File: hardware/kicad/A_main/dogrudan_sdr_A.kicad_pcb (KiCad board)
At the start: 6 copper layers, 235 x 225 mm, 264 parts, among them J1 XT60, J10 JTAG 2x3, J20 SMA A1, J21 SMA B1, J22 SMA A2, J23 SMA B2, J30 SMA TX1, J31 SMA TX2, J32 SMA TX3, J33 SMA TX4, J40 HR911130A, J41 HR911130A, J60 GPS modul, J61 SMA 10MHz ref, J62 DAC modul, J63 C kartina, J64 UART 3.3V, J65 C kartina #2, J66 D kartina, Q1 DMP3098L, SW1 PROG, T1 ADT1-1WT+, T10 ADT1-1WT+, T11 ADT1-1WT+, T12 ADT1-1WT+, T13 ADT1-1WT+, T2 ADT1-1WT+, T3 ADT1-1WT+, T4 ADT1-1WT+, U1 TPS62130, U10 LFE5U-25F-7BG256I, U11 W25Q128JVSIQ, U15 ADCLK846BCPZ, U16 SN65LVDS2DBVR, U17 SN65LVDS2DBVR, U2 TPS62130, U20 AD9251BCPZ-80, U21 AD9251BCPZ-80, U3 TPS7A2033, U30 AD9767ASTZ, U31 AD9767ASTZ, U4 ADP150, U40 RTL8211FI-CG, U41 RTL8211FI-CG, U5 ADP150, U50 W9825G6KH-6I, U6 ADP150, U62 TLV3501AIDBVR, U7 ADP150, U8 ADP150, U9 ADP150, Y10 ABLNO-V-80.000MHZ, Y610 25MHz, Y626 25MHz

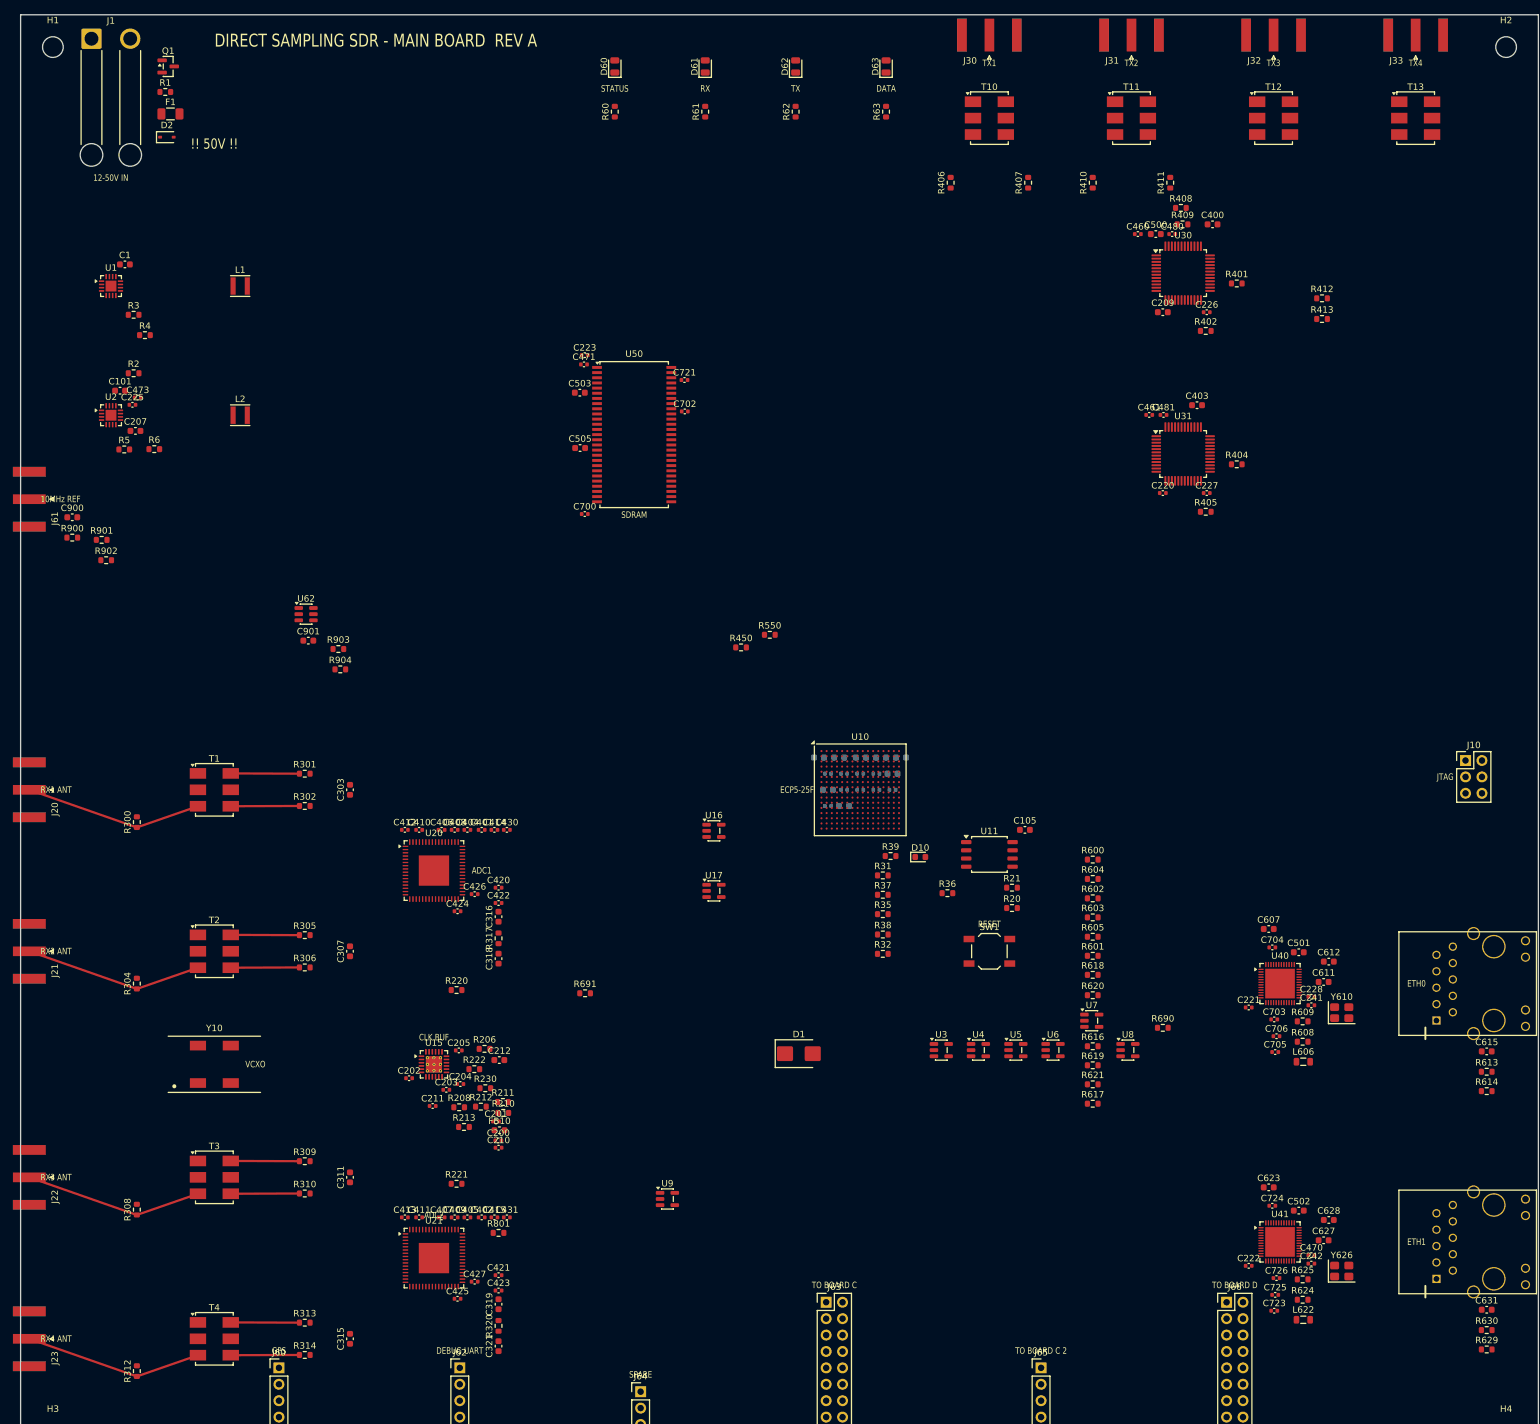
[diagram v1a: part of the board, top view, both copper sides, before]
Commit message: Connect the pads that had no net
A symbol pin number must agree with the footprint pad number. If the
numbers do not agree, the net goes nowhere. The netlist removes it
and gives no message. ERC examines the schematic and sees a wire. DRC
does not count an unconnected pad as a violation. All three boards
showed zero ERC violations while 31 pads had no net.

Two of these faults stopped a board.

The footprint of the Ethernet PHY was for a different part. The
project used QFN-48 6x6 mm with 0.4 mm pitch. The RTL8211F(I)-CG is
WQFN-40-EP 5x5 mm. You cannot solder the part to that pad pattern.

The 25 MHz crystal had a 2-pin symbol on a 4-pad footprint. On a 3225
crystal the terminals are the diagonal pads 1 and 3. Pads 2 and 4 are
the metal can. XO went to pad 2. There was no crystal between XI and
XO, and thus neither PHY could make a clock.

The paddle of the AD9251 was pin 0 in the symbol and pad 65 in the
footprint. The paddle of the PE4312 was Pad against pad 21. The gas
discharge tubes had one electrode unconnected, because
Device:GDT_2Pin uses pins 1 and 3 but the varistor footprint uses
pads 1 and 2. A local footprint with pads 1 and 3 corrects this.

ped_denetim.py finds these faults on the board. yap.sh runs it before
the DSN export. The chain stops if a pad has no net.

The DSN export also changed. It declared In1 and In4 as power layers
but did not export the copper on them. The router thus believed that
the two ground planes were empty. It routed the 289 pins of GND as
traces on the signal layers. The planes now go out as conduction
areas.
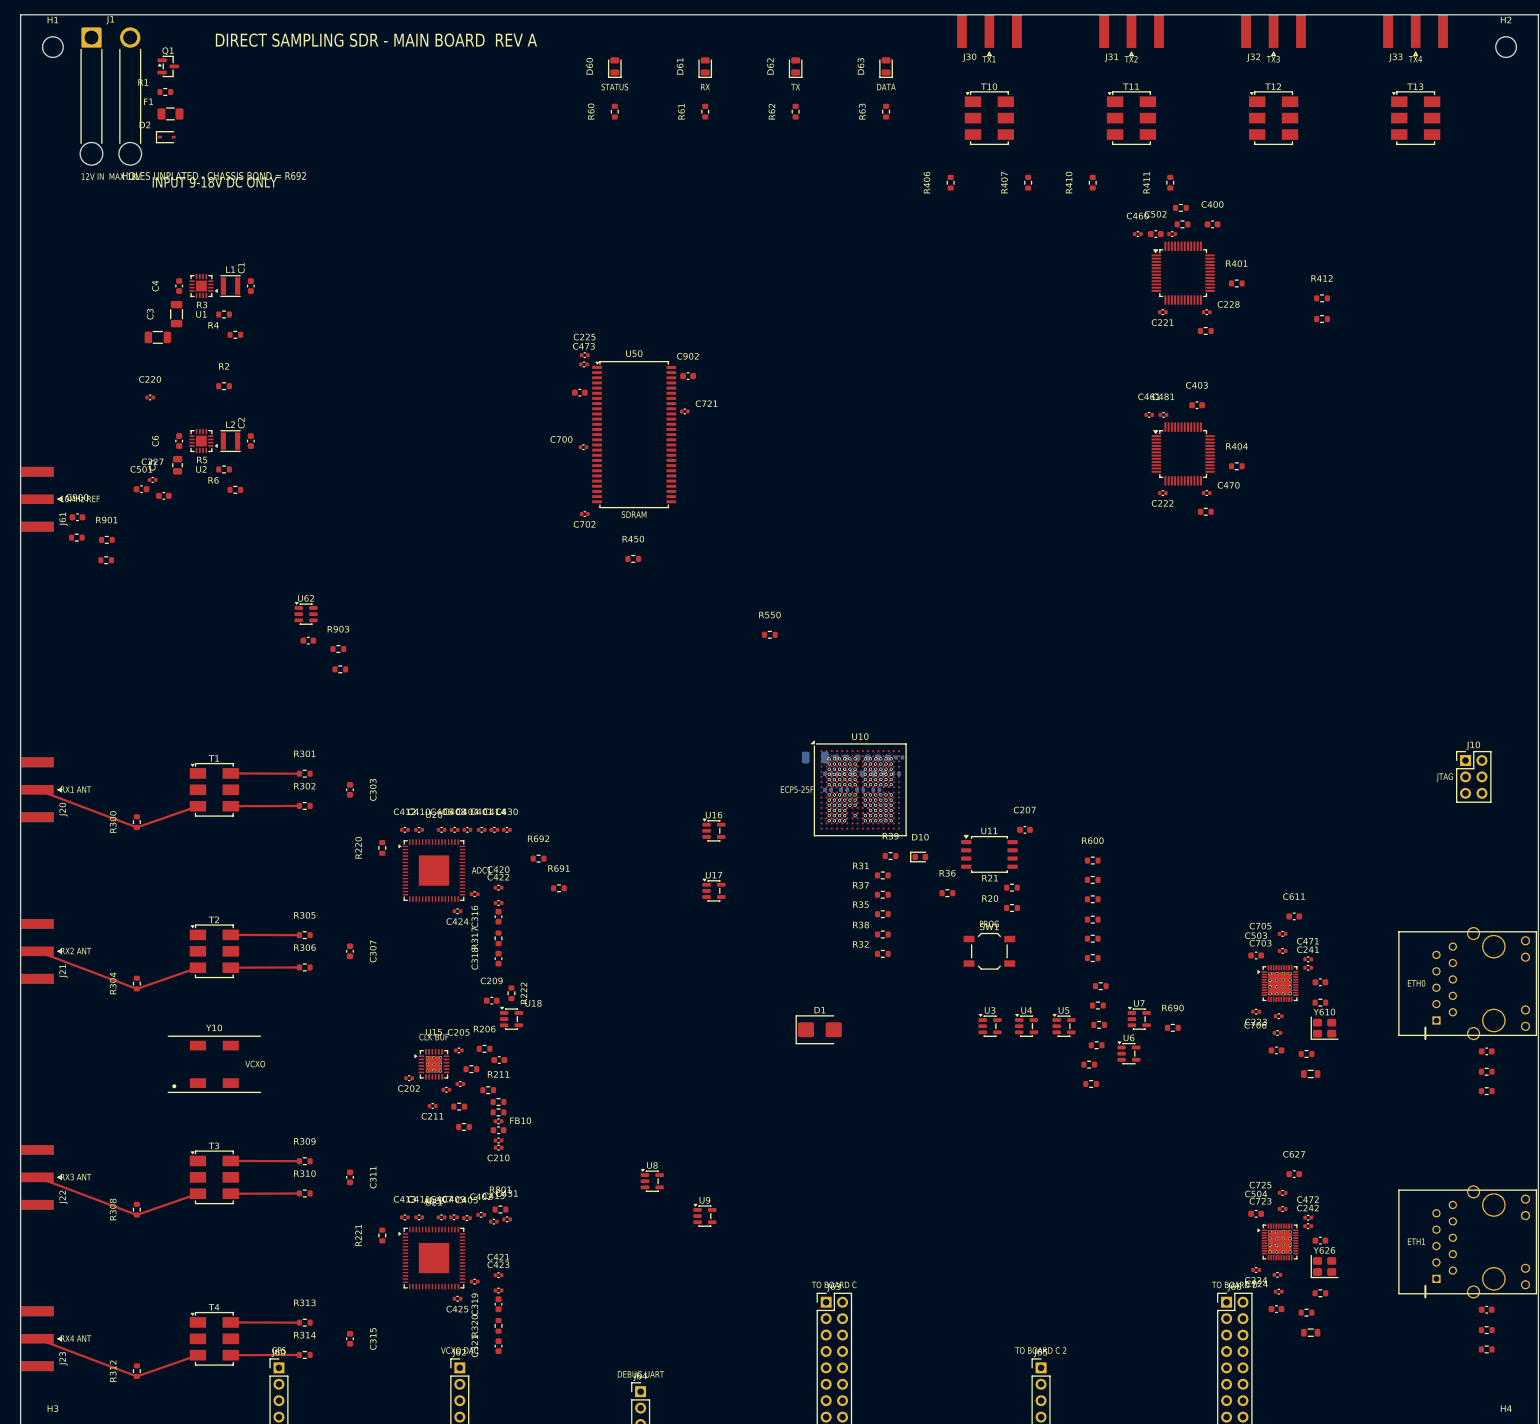
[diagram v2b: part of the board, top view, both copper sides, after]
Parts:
- added C3: 10uF, C_1206_3216Metric, F.Cu at (24.1, 46.4)
- added C4: 100nF, C_0603_1608Metric, F.Cu at (24.6, 42.0)
- added C5: 10uF, C_0805_2012Metric, F.Cu at (24.3, 69.8)
- added C6: 100nF, C_0603_1608Metric, F.Cu at (24.6, 66.0)
- added R692: 0R, R_0603_1608Metric, F.Cu at (80.2, 130.7)
- added U18: SN65LVDS2DBVR, SOT-23-5, F.Cu at (76.0, 155.5)
- C100: footprint C_0603_1608Metric -> C_1206_3216Metric
- C104: footprint C_0603_1608Metric -> C_1206_3216Metric; moved to F.Cu
- C105, C226, C500: moved to B.Cu
- C2, C224, C472, C504, C902: moved to F.Cu
- U40, U41: footprint QFN-48-1EP_6x6mm_P0.4mm_EP4.6x4.6mm -> QFN-40-1EP_5x5mm_P0.4mm_EP3.6x3.6mm_ThermalVias
- moved C501 193.0 mm to (18.7, 73.5)
- moved C227 163.2 mm to (20.5, 72.0)
- moved C220 157.5 mm to (20.1, 59.2)
- moved C502 152.8 mm to (175.8, 34.0)
- moved C207 150.9 mm to (155.5, 126.2)
- moved C209 148.9 mm to (73.0, 152.7)
- moved C223 145.4 mm to (191.3, 154.3)
- moved C471 145.1 mm to (199.3, 146.2)
- moved C503 136.2 mm to (191.3, 145.7)
- moved C104 129.5 mm to (21.2, 50.0)
- moved C222 120.4 mm to (176.8, 74.0)
- moved C470 119.1 mm to (183.7, 74.0)
- moved C2 112.0 mm to (35.6, 66.0), turned to 90 degrees
- moved C221 108.5 mm to (176.8, 46.0)
- moved C228 107.2 mm to (183.7, 46.0)
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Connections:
- J40 pad SH1: (no net) -> CHASSIS
- J40 pad SH2: (no net) -> CHASSIS
- J40 pad SH3: (no net) -> CHASSIS
- J40 pad SH4: (no net) -> CHASSIS
- J41 pad SH1: (no net) -> CHASSIS
- J41 pad SH2: (no net) -> CHASSIS
- J41 pad SH3: (no net) -> CHASSIS
- J41 pad SH4: (no net) -> CHASSIS
- U10 pad K16: LED_RX -> FPGA_CLK80
- U10 pad R6: unconnected-(U10H-D6/PB4B-PadR6) -> LED_RX
- U20 pad 65: (no net) -> GND
- U21 pad 65: (no net) -> GND
- U30 pad 1: DAC1_P1_D0 -> DAC1_P1_D13
- U30 pad 10: DAC1_P1_D9 -> DAC1_P1_D4
- U30 pad 11: DAC1_P1_D10 -> DAC1_P1_D3
- U30 pad 12: DAC1_P1_D11 -> DAC1_P1_D2
- U30 pad 13: DAC1_P1_D12 -> DAC1_P1_D1
- U30 pad 14: DAC1_P1_D13 -> DAC1_P1_D0
- U30 pad 2: DAC1_P1_D1 -> DAC1_P1_D12
- U30 pad 3: DAC1_P1_D2 -> DAC1_P1_D11
- U30 pad 4: DAC1_P1_D3 -> DAC1_P1_D10
- U30 pad 5: DAC1_P1_D4 -> DAC1_P1_D9
- U30 pad 6: DAC1_P1_D5 -> DAC1_P1_D8
- U30 pad 7: DAC1_P1_D6 -> DAC1_P1_D7
- U30 pad 8: DAC1_P1_D7 -> DAC1_P1_D6
- U30 pad 9: DAC1_P1_D8 -> DAC1_P1_D5
- U31 pad 1: DAC2_D0 -> DAC2_D13
- U31 pad 10: DAC2_D9 -> DAC2_D4
- U31 pad 11: DAC2_D10 -> DAC2_D3
- U31 pad 12: DAC2_D11 -> DAC2_D2
- U31 pad 13: DAC2_D12 -> DAC2_D1
- U31 pad 14: DAC2_D13 -> DAC2_D0
- U31 pad 2: DAC2_D1 -> DAC2_D12
- U31 pad 3: DAC2_D2 -> DAC2_D11
- U31 pad 4: DAC2_D3 -> DAC2_D10
- U31 pad 5: DAC2_D4 -> DAC2_D9
- U31 pad 6: DAC2_D5 -> DAC2_D8
- U31 pad 7: DAC2_D6 -> DAC2_D7
- U31 pad 8: DAC2_D7 -> DAC2_D6
- U31 pad 9: DAC2_D8 -> DAC2_D5
- Y610 pad 2: PHY1_XO -> GND
- Y610 pad 3: (no net) -> PHY1_XO
- Y610 pad 4: (no net) -> GND
- Y626 pad 2: PHY2_XO -> GND
- Y626 pad 3: (no net) -> PHY2_XO
- Y626 pad 4: (no net) -> GND
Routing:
- net GND: track 0.00 -> 8.49 mm, vias 0 -> 15
- net +3V3: track 0.00 -> 5.09 mm, vias 0 -> 9
- net +1V1: track 0.00 -> 3.39 mm, vias 0 -> 6
- net +1V8: track 0.00 -> 2.26 mm, vias 0 -> 4
- net RF_B2: track 27.7 -> 26.5 mm
- net RF_B1: track 27.7 -> 26.5 mm
- net RF_A2: track 27.7 -> 26.5 mm
- net RF_A1: track 27.7 -> 26.5 mm
- net +2V5: track 0.00 -> 1.13 mm, vias 0 -> 2
- net VCXO_DIN: track 0.00 -> 0.57 mm, vias 0 -> 1
- net VCXO_CLK: track 0.00 -> 0.57 mm, vias 0 -> 1
- net TR4: track 0.00 -> 0.57 mm, vias 0 -> 1
- net TR3: track 0.00 -> 0.57 mm, vias 0 -> 1
- net TR1: track 0.00 -> 0.57 mm, vias 0 -> 1
- net SD_DQ15: track 0.00 -> 0.57 mm, vias 0 -> 1
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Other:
- board text added: "​12V IN MAX 18V"
- board text added: "​HOLES UNPLATED - CHASSIS BOND = R692"
- board text added: "​INPUT 9-18V DC ONLY"
- board text added: "​PROG"
- board text added: "​VCXO DAC"
- board text removed: "​!! 50V !!"
- board text removed: "​12-50V IN"
- board text removed: "​RESET"
- board text removed: "​SPARE"
